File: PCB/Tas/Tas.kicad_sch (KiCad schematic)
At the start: 26 parts, among them J1 Shelly 1, J2 Conn_01x07, J3 USB-C, Q1 PMF170XP,115, Q2 PMF250XNEX, U1 FT231XQ, U2 LMR16006YDDCR

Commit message: Tidy
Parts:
- Art2: footprint RevK:QR-Tas -> RevK:QR-TAS
- D1, D2: footprint RevK:SOT-363_SC-70-6-Rot -> RevK:SOT-363_SC-70-6

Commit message: Fix rotation
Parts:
- D1, D2: JLCPCB Rotation Offset (none) -> -90
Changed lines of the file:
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@@
+      (effects (font (size 1.27 1.27)) hide)
+    )
+    (property "JLCPCB Rotation Offset" "-90" (at 78.74 98.425 0)
       (effects (font (size 1.27 1.27)) hide)
     )
@@
       (effects (font (size 1.27 1.27)) hide)
     )
+    (property "JLCPCB Rotation Offset" "-90" (at 78.74 117.475 0)
+      (effects (font (size 1.27 1.27)) hide)
+    )
     (pin "1")
     (pin "2")
@@
       (effects (font (size 1.27 1.27)) hide)
     )
+    (property "JLCPCB Rotation Offset" "-90" (at 78.74 139.7 0)
+      (effects (font (size 1.27 1.27)) hide)
+    )
     (pin "1")
     (pin "2")
@@
       (effects (font (size 1.27 1.27)) hide)
     )
+    (property "JLCPCB Rotation Offset" "-90" (at 79.375 163.195 0)
+      (effects (font (size 1.27 1.27)) hide)
+    )

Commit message: Replaced old board with new
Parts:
- removed C2: 100nF, RevK:C_0603_, symbol RevK:Hidden
- removed C3: 2.2uF, RevK:C_0805_, symbol RevK:Hidden
- removed C4: 10uF, RevK:C_0805_, symbol RevK:Hidden
- removed D3: LED, LED_SMD:LED_0603_1608Metric_Pad1.05x0.95mm_HandSolder, symbol Device:LED
- removed D4: Schottky, RevK:D_1206_, symbol RevK:Hidden
- removed L1: 6.8uH, RevK:L_4x4_, symbol RevK:Hidden
- removed R5: 680R, RevK:R_0603, symbol Device:R
- removed U2: LMR16006YDDCR, RevK:SOT-23-Thin-6-Reg, symbol RevK:LMR16006XDDCR
- added C6: 10uF 50V, RevK:C_0603_, symbol RevK:Hidden
- added C7: 10uF 6.3V, RevK:C_0603_, symbol RevK:Hidden
- added C8: 100nF, RevK:C_0603_, symbol RevK:Hidden
- added D4: RGB, RevK:LED-RGB-1.6x1.6, symbol Device:LED_RGBA
- added L2: 10uH, RevK:L_4x4_, symbol RevK:Hidden
- added R10: 1M, RevK:R_0402_, symbol RevK:Hidden
- added R11: 220R, RevK:R_0402, symbol Device:R
- added R8: 124k, RevK:R_0402_, symbol RevK:Hidden
- added R9: 39k2, RevK:R_0402_, symbol RevK:Hidden
- added U3: MD8942, RevK:SOT-23-6-MD8942, symbol RevK:MD89420-RegBlock
- C1, C5: footprint RevK:C_0603 -> RevK:C_0402
- R1, R2, R3, R4: footprint RevK:R_0603 -> RevK:R_0402
- R6: value 100k 1% -> 680R; footprint RevK:R_0603 -> RevK:R_0402; LCSC Part # C14675 -> (none)
- R7: value 30k 1% -> 2K; footprint RevK:R_0603 -> RevK:R_0402; LCSC Part # C100001 -> (none)
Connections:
- net +3V3: now also D4.4 (A), U3.8 (VOUT); no longer R6.1
- net GND: now also U3.2 (GND), U3.7 (GND); no longer R7.1
- net VBUS: now also U3.5 (VIN)
- net at U1.14 (CBUS1): now also R7.2
- net at U1.15 (CBUS0): now also R6.2
- net at U1.16 (CBUS3): now also R11.2
- new net: D4.1 (RK), R6.1
- new net: D4.2 (GK), R7.1
- new net: D4.3 (BK), R11.1
- no-connect marks 4 -> 3
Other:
- note added: "Configure FTDI - Inverted RTS - CBUS modes for LEDs, suggest :- - CBUS0 mode 1 - CBUS1 mode 2 - CBUS3 mode 9"
- note removed: "Configure FTDI - Inverted RTS - CBUS0 mode 9"
- note removed: "Note, a better regulator for this may be the TLV62569 as it is suitable up to 5.5V input and small footprint."
- moved on the sheet: C1, C5, U1

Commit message: New reg
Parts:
- removed Art2: QR, RevK:QR-TAS, symbol RevK:QR
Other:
- moved on the sheet: R3, R4
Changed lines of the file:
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@@
     (stroke (width 0) (type default))
   )
-  (wire (pts (xy 179.07 60.96) (xy 184.15 60.96))
+  (wire (pts (xy 163.83 60.96) (xy 168.91 60.96))
     (stroke (width 0) (type default))
   )
@@
     (stroke (width 0) (type default))
   )
-  (wire (pts (xy 153.67 63.5) (xy 171.45 63.5))
-    (stroke (width 0) (type default))
-  )
-  (wire (pts (xy 179.07 63.5) (xy 184.15 63.5))
+  (wire (pts (xy 153.67 63.5) (xy 156.21 63.5))
+    (stroke (width 0) (type default))
+  )
+  (wire (pts (xy 163.83 63.5) (xy 168.91 63.5))
     (stroke (width 0) (type default))
   )
@@
     (stroke (width 0) (type default))
   )
-  (wire (pts (xy 153.67 60.96) (xy 171.45 60.96))
+  (wire (pts (xy 153.67 60.96) (xy 156.21 60.96))
     (stroke (width 0) (type default))
   )
@@
     )
   )
-  (global_label "D-" (shape input) (at 184.15 60.96 0) (fields_autoplaced)
+  (global_label "D-" (shape input) (at 168.91 60.96 0) (fields_autoplaced)
     (effects (font (size 1.27 1.27)) (justify left))
-    (property "Intersheetrefs" "${INTERSHEET_REFS}" (at -25.4 15.24 0)
+    (property "Intersheetrefs" "${INTERSHEET_REFS}" (at -40.64 15.24 0)
       (effects (font (size 1.27 1.27)) hide)
     )
@@
     )
   )
-  (global_label "D+" (shape input) (at 184.15 63.5 0) (fields_autoplaced)
+  (global_label "D+" (shape input) (at 168.91 63.5 0) (fields_autoplaced)
     (effects (font (size 1.27 1.27)) (justify left))
-    (property "Intersheetrefs" "${INTERSHEET_REFS}" (at -25.4 12.7 0)
+    (property "Intersheetrefs" "${INTERSHEET_REFS}" (at -40.64 12.7 0)
       (effects (font (size 1.27 1.27)) hide)
     )
@@
     )
   )
-  (symbol (lib_id "Device:R") (at 175.26 60.96 90) (unit 1)
-    (in_bom yes) (on_board yes) (dnp no)
-    (property "Reference" "R3" (at 175.26 58.42 90)
-      (effects (font (size 1.27 1.27)))
-    )
-    (property "Value" "27R" (at 175.26 60.96 90)
-      (effects (font (size 1.27 1.27)))
-    )
-    (property "Footprint" "RevK:R_0402" (at 175.26 62.738 90)
-      (effects (font (size 1.27 1.27)) hide)
-    )
-    (property "Datasheet" "~" (at 175.26 60.96 0)
+  (symbol (lib_id "Device:R") (at 160.02 60.96 90) (unit 1)
+    (in_bom yes) (on_board yes) (dnp no)
+    (property "Reference" "R3" (at 160.02 58.42 90)
+      (effects (font (size 1.27 1.27)))
+    )
+    (property "Value" "27R" (at 160.02 60.96 90)
+      (effects (font (size 1.27 1.27)))
+    )
+    (property "Footprint" "RevK:R_0402" (at 160.02 62.738 90)
+      (effects (font (size 1.27 1.27)) hide)
+    )
+    (property "Datasheet" "~" (at 160.02 60.96 0)
       (effects (font (size 1.27 1.27)) hide)
     )
@@
     )
   )
-  (symbol (lib_id "Device:R") (at 175.26 63.5 90) (unit 1)
-    (in_bom yes) (on_board yes) (dnp no)
-    (property "Reference" "R4" (at 175.26 66.04 90)
-      (effects (font (size 1.27 1.27)))
-    )
-    (property "Value" "27R" (at 175.26 63.5 90)
-      (effects (font (size 1.27 1.27)))
-    )
-    (property "Footprint" "RevK:R_0402" (at 175.26 65.278 90)
-      (effects (font (size 1.27 1.27)) hide)
-    )
-    (property "Datasheet" "~" (at 175.26 63.5 0)
+  (symbol (lib_id "Device:R") (at 160.02 63.5 90) (unit 1)
+    (in_bom yes) (on_board yes) (dnp no)
+    (property "Reference" "R4" (at 160.02 66.04 90)
+      (effects (font (size 1.27 1.27)))
+    )
+    (property "Value" "27R" (at 160.02 63.5 90)
+      (effects (font (size 1.27 1.27)))
+    )
+    (property "Footprint" "RevK:R_0402" (at 160.02 65.278 90)
+      (effects (font (size 1.27 1.27)) hide)
+    )
+    (property "Datasheet" "~" (at 160.02 63.5 0)
       (effects (font (size 1.27 1.27)) hide)
     )
@@
         )
       )
-    )
-  )
-  (symbol (lib_id "RevK:QR") (at 271.78 172.72 0) (unit 1)
-    (in_bom no) (on_board yes) (dnp no)
-    (property "Reference" "Art2" (at 271.78 175.895 0)
-      (effects (font (size 1.27 1.27)) hide)
-    )
-    (property "Value" "QR" (at 271.78 175.895 0)
-      (effects (font (size 1.27 1.27)) hide)
-    )
-    (property "Footprint" "RevK:QR-TAS" (at 271.145 173.355 0)
-      (effects (font (size 1.27 1.27)) hide)
-    )
-    (property "Datasheet" "" (at 271.145 173.355 0)
-      (effects (font (size 1.27 1.27)) hide)
-    )
-    (property "Note" "Non part, PCB printed" (at 271.78 172.72 0)
-      (effects (font (size 1.27 1.27)) hide)
-    )
-    (instances
-      (project "Tas"
-        (path "/42713045-fffd-4b2d-ae1e-7232d705fb12"
-          (reference "Art2") (unit 1)
-        )
-      )

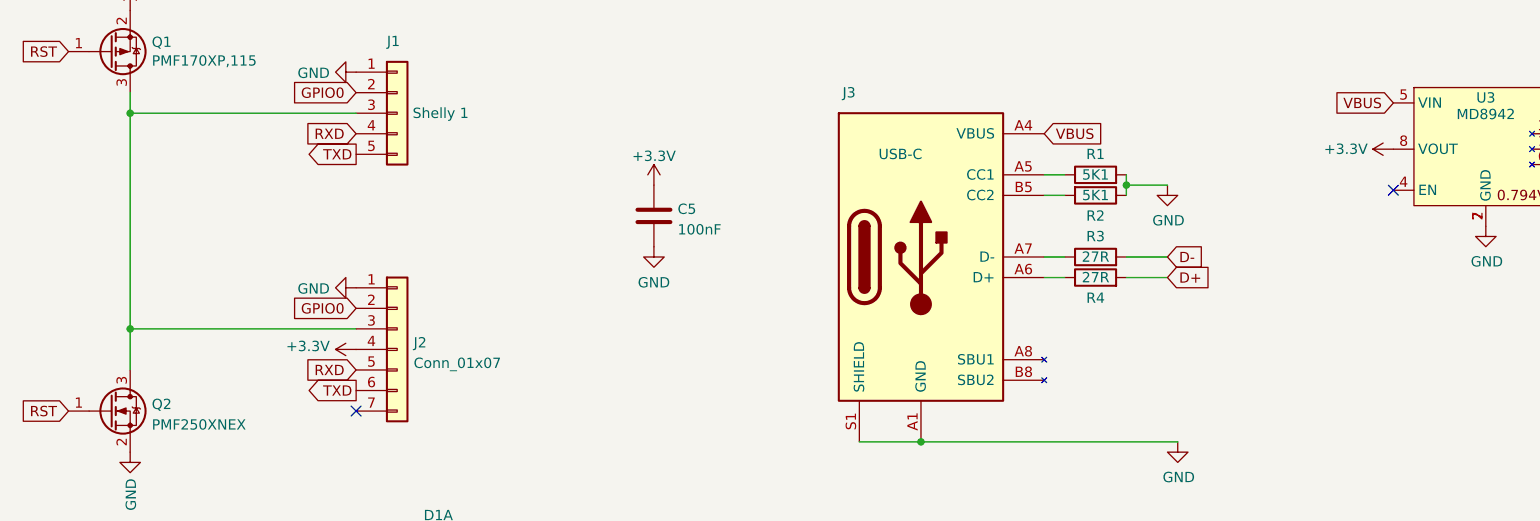
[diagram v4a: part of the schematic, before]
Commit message: More caps
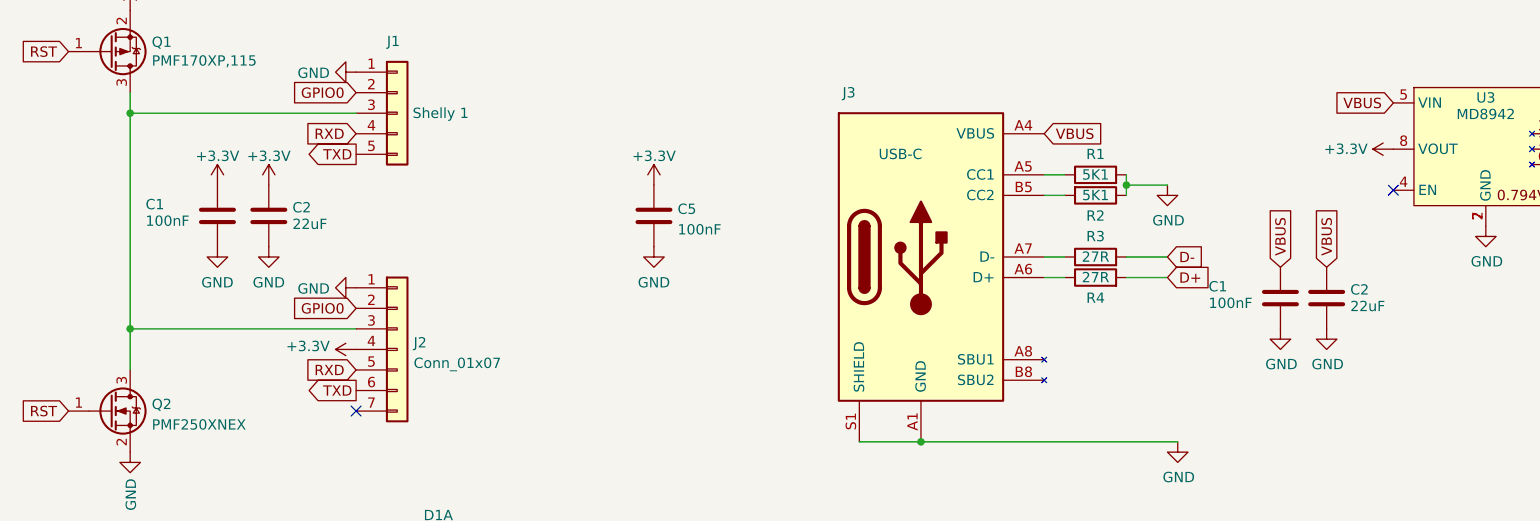
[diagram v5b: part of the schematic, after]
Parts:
- added C1 (x2): 100nF, RevK:C_0402, symbol Device:C
- added C2 (x2): 22uF, RevK:C_0603, symbol Device:C
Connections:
- net +3V3: now also C1.1, C2.1
- net GND: now also C1.2, C1.2, C2.2, C2.2
- net VBUS: now also C1.1, C2.1

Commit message: Tidy
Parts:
- removed J3: USB-C, RevK:USC16-TR, symbol RevK:USB-C
- added C27: 100uF 6.3V, RevK:C_1206, symbol Device:C
- added J3: USB-C-Socket-V, RevK:USB-C-Socket-H, symbol RevK:USB-C-Socket-H
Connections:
- net GND: now also C27.1, J3.A1 (GND), J3.A12 (GND), J3.B1 (GND), J3.B12 (GND), J3.S1 (SHIELD)
- net VBUS: now also C27.2, J3.A4 (VBUS), J3.A9 (VBUS), J3.B4 (VBUS), J3.B9 (VBUS)
- net at R1.1: now also J3.A5 (CC1)
- net at R4.1: now also J3.A6 (D+), J3.B6 (D+)
- net at R3.1: now also J3.A7 (D-), J3.B7 (D-)
- net at R2.2: now also J3.B5 (CC2)
- net +3V3 renamed +3.3V
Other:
- moved on the sheet: C1, C2

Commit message: Tidy
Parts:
- removed D1, D2: BAV99S, RevK:SOT-363_SC-70-6, symbol Diode:BAV99S
- added D1, D2, D3, D5: ~, RevK:DFN1006-2L, symbol RevK:ES05D1MC10
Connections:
- net GND: now also D1.2, D2.2, D3.2, D5.2
- net GPIO0: now also D2.1
- net RST: now also D1.1
- net RXD: now also D5.1
- net TXD: now also D3.1

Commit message: Tidy
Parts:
- added PCB1: 70x70, RevK:PCB7070, symbol RevK:PCB
- added V2, V3: ~, RevK:VCUT70N, symbol RevK:VCUT
- C6: value 10uF 50V -> 10uF 35V; LCSC Part # C1591 -> C194427
